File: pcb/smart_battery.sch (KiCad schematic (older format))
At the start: 35 parts, among them J11 Conn_01x05_RTC, J12 Conn_HtrTh, J13 Conn_BattTh, Q1 MMBT5551L, Q2 MMBT5551L, U1 SPX3819M5-L-3-3, U10 FEATHER_M0_ADALOGGER, U11 FEATHERWING_HEATER_RELAY, U12 FEATHERWING_ETHERNET, U13 FEATHERWING_MINI_RELAY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

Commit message: Laying out board
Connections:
- net GND: no longer JP2.2 (Pin_2)
- net SOLPWR: now also JP2.2 (Pin_2)
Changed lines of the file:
@@
 	2950 4400 2950 4000
 Wire Wire Line
-	2950 4000 3250 4000
-Wire Wire Line
-	3200 4100 3250 4100
-Wire Wire Line
-	3200 3850 3200 4100
+	2950 4000 3100 4000
 $Comp
 L Connector:Screw_Terminal_01x02 JP3
@@
 Wire Wire Line
 	2950 5900 3200 5900
-Wire Wire Line
-	3150 5750 3150 6000
-Wire Wire Line
-	3150 6000 3200 6000
 Connection ~ 3150 5750
 Wire Wire Line
 	3150 5750 3200 5750
 Wire Wire Line
-	3200 4100 3200 4200
-Wire Wire Line
 	3200 4200 3250 4200
-Connection ~ 3200 4100
-Wire Wire Line
-	3150 6000 3150 6100
 Wire Wire Line
 	3150 6100 3200 6100
-Connection ~ 3150 6000
 Text Label 4650 900  2    50   ~ 0
 VBAT
@@
 Wire Wire Line
 	1300 3650 1200 3650
+Wire Wire Line
+	3200 3850 3200 4200
+Wire Wire Line
+	3100 4000 3100 4100
+Wire Wire Line
+	3100 4100 3250 4100
+Connection ~ 3100 4000
+Wire Wire Line
+	3100 4000 3250 4000
+Wire Wire Line
+	3150 6000 3150 6100
+Wire Wire Line
+	3150 5750 3150 6000
+Connection ~ 3150 6000
+Wire Wire Line
+	3150 6000 3200 6000
 $EndSCHEMATC

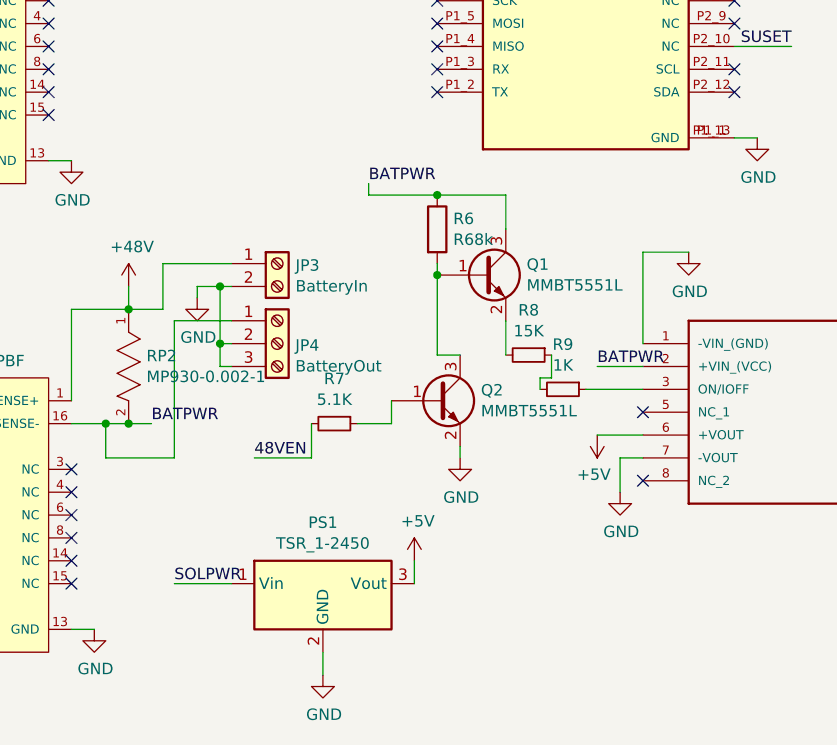
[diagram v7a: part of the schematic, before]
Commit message: Added diodes to protect battery inputs
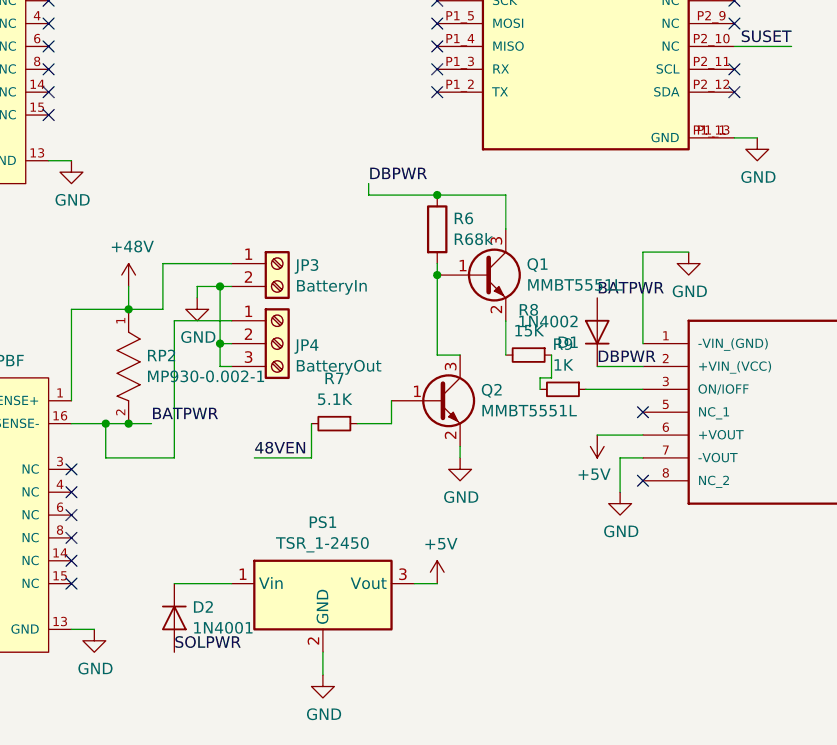
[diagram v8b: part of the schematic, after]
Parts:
- added D1: 1N4002, Diode_THT:D_DO-41_SOD81_P10.16mm_Horizontal, symbol Diode:1N4002
- added D2: 1N4001, Diode_THT:D_DO-41_SOD81_P10.16mm_Horizontal, symbol Diode:1N4001
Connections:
- net BATPWR: now also D1.2 (A); no longer PS2.2 (+VIN_(VCC)), Q1.3 (C), R6.1
- net SOLPWR: now also D2.2 (A); no longer PS1.1 (Vin)
- new net: D2.1 (K), PS1.1 (Vin)
- new net DBPWR: D1.1 (K), PS2.2 (+VIN_(VCC)), Q1.3 (C), R6.1
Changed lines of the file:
@@
 L power:+5V #PWR019
 U 1 1 601CCD37
-P 4000 6950
-F 0 "#PWR019" H 4000 6800 50  0001 C CNN
-F 1 "+5V" H 4015 7123 50  0000 C CNN
-F 2 "" H 4000 6950 50  0001 C CNN
-F 3 "" H 4000 6950 50  0001 C CNN
-	1    4000 6950
-	1    0    0    -1
-$EndComp
-Wire Wire Line
-	4000 6950 4000 7050
+P 4100 7050
+F 0 "#PWR019" H 4100 6900 50  0001 C CNN
+F 1 "+5V" H 4115 7223 50  0000 C CNN
+F 2 "" H 4100 7050 50  0001 C CNN
+F 3 "" H 4100 7050 50  0001 C CNN
+	1    4100 7050
+	1    0    0    -1
+$EndComp
 $Comp
 L TEC_2-2411:TEC_2-2411 PS2
@@
 	2850 6350 2750 6350
 Connection ~ 2750 6350
-Text Label 4800 6100 0    50   ~ 0
+Text Label 4800 5800 0    50   ~ 0
 BATPWR
 Text Label 2850 6350 0    50   ~ 0
@@
 	2750 4300 2650 4300
 Connection ~ 2650 4300
-Text Label 2950 7050 0    50   ~ 0
+Text Label 2950 7350 0    50   ~ 0
 SOLPWR
 Wire Wire Line
@@
 	1    0    0    -1
 $EndComp
-Text Label 3800 5300 0    50   ~ 0
-BATPWR
 Wire Wire Line
 	3800 5300 3800 5350
@@
 Wire Wire Line
 	3150 6000 3200 6000
+$Comp
+L Diode:1N4001 D2
+U 1 1 60267D7A
+P 2950 7200
+F 0 "D2" V 2904 7279 50  0000 L CNN
+F 1 "1N4001" V 2995 7279 50  0000 L CNN
+F 2 "Diode_THT:D_DO-41_SOD81_P10.16mm_Horizontal" H 2950 7025 50  0001 C CNN
+F 3 "http://www.vishay.com/docs/88503/1n4001.pdf" H 2950 7200 50  0001 C CNN
+	1    2950 7200
+	0    1    1    0
+$EndComp
+$Comp
+L Diode:1N4002 D1
+U 1 1 602681D6
+P 4800 5950
+F 0 "D1" V 4754 6029 50  0000 L CNN
+F 1 "1N4002" V 4845 6029 50  0000 L CNN
+F 2 "Diode_THT:D_DO-41_SOD81_P10.16mm_Horizontal" H 4800 5775 50  0001 C CNN
+F 3 "http://www.vishay.com/docs/88503/1n4001.pdf" H 4800 5950 50  0001 C CNN
+	1    4800 5950
+	0    -1   -1   0
+$EndComp
+Wire Wire Line
+	4000 7050 4100 7050
+Text Label 3800 5300 0    50   ~ 0
+DBPWR
+Text Label 4800 6100 0    50   ~ 0
+DBPWR
 $EndSCHEMATC
